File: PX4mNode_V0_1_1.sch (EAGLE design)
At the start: 128 parts, among them J201 DF13C-6P-1.25V, J202 DF13C-6P-1.25V, J203 DF13C-6P-1.25V, J301 DF13C-4P-1.25V, J401 DF13C-7P-1.25V, J402 DF13-4P-1.25V, J403 DF13C-4P-1.25V, J404 DF13C-4P-1.25V, J405 DF13C-4P-1.25V, J801 DF13C-3P-1.25V, M3_MOUNT1101 MOUNT-HOLE3.1MM, M3_MOUNT1102 MOUNT-HOLE3.1MM, M3_MOUNT1103 MOUNT-HOLE3.1MM, M3_MOUNT1104 MOUNT-HOLE3.1MM, U101 STM32F4X7VX, U401 MAX3051, U402 MAX3051, X101 3.2x2.5 mm / 24 MHz / 15 ppm

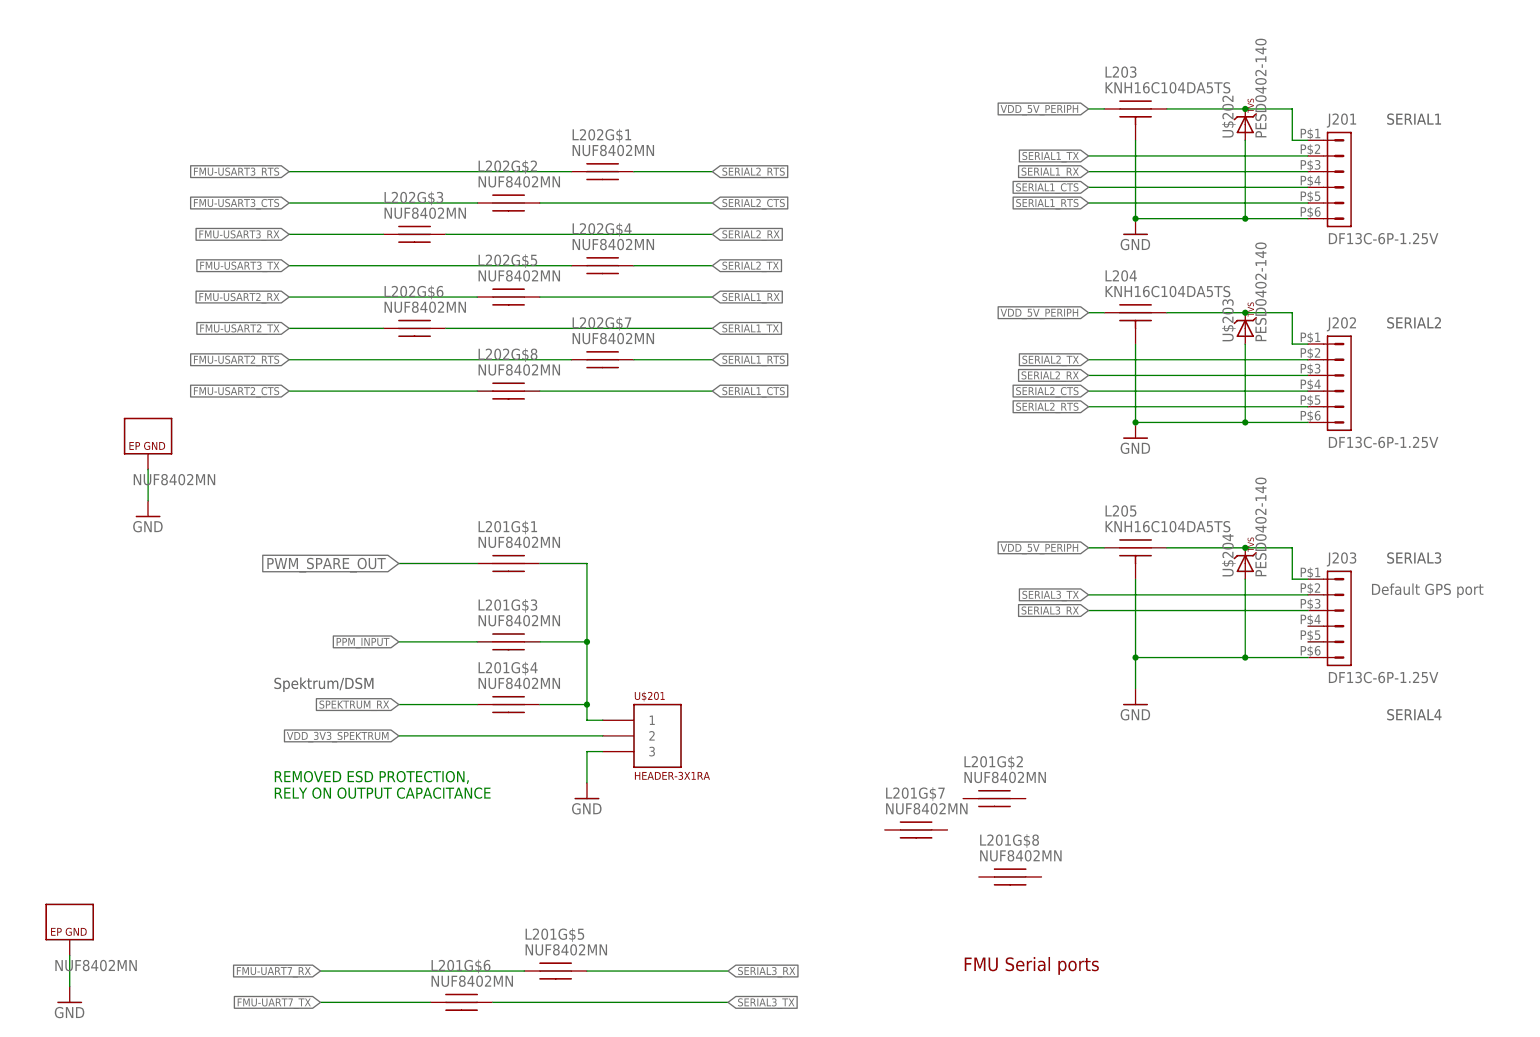
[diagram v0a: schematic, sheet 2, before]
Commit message: Added SBUS input inverter
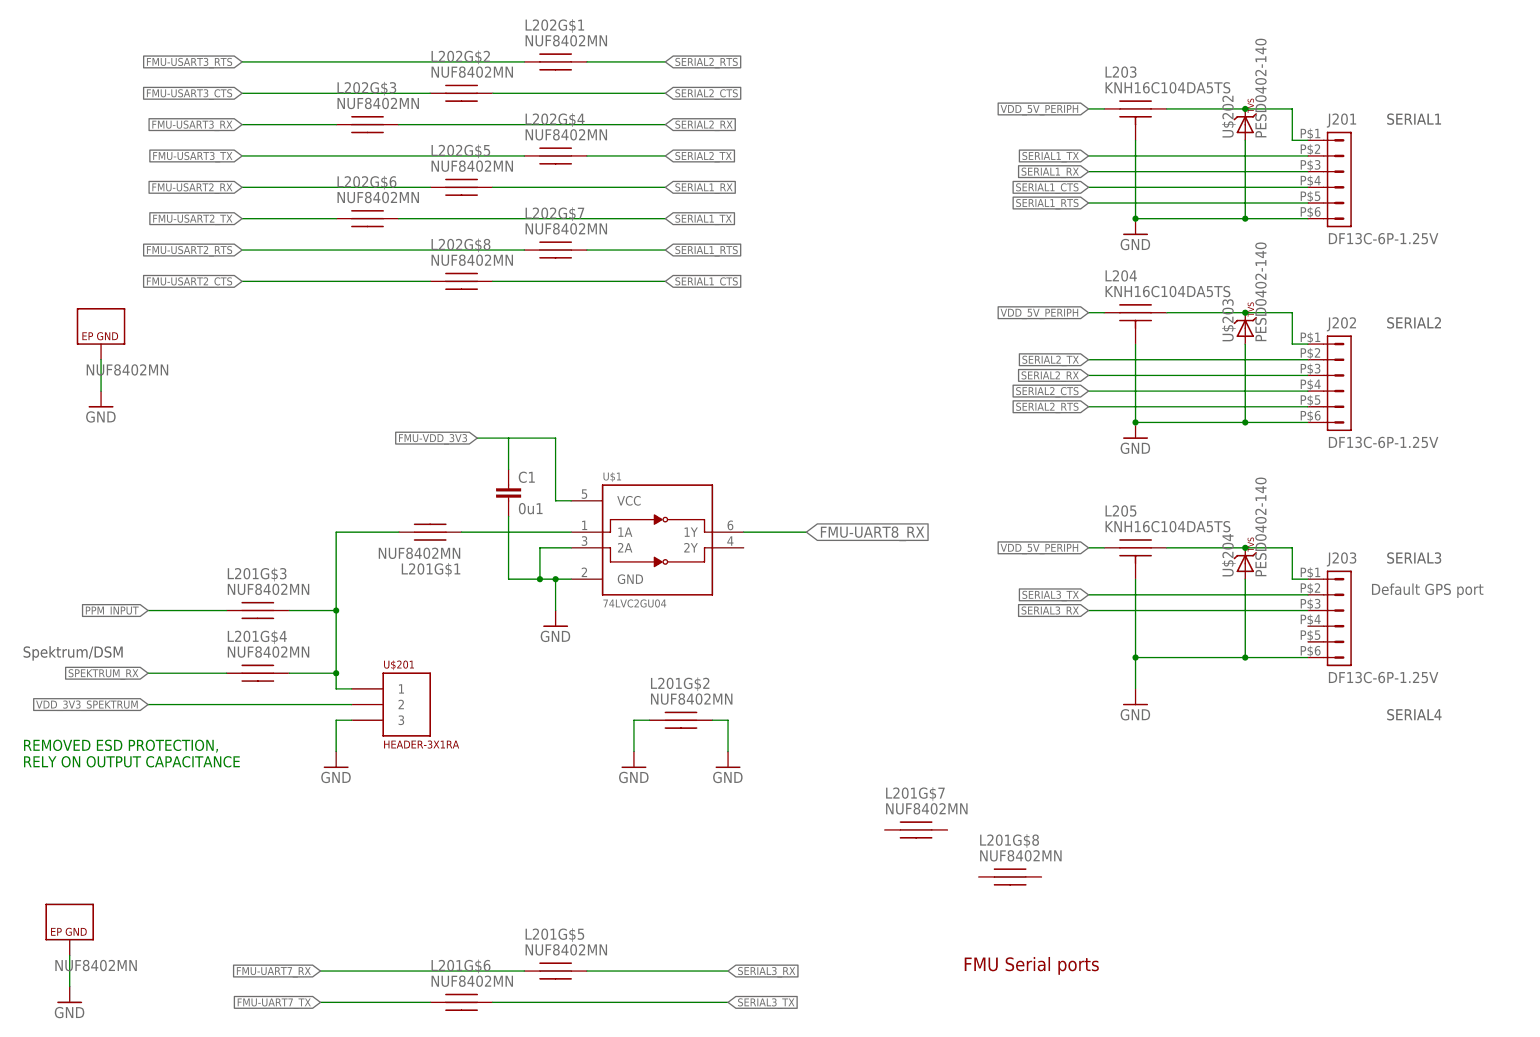
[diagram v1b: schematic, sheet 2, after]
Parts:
- added C1: 0u1, pixhawk2:CAP0402
- added U$1: 74LVC2GU04, pixhawk2:74LVC2GU04
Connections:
- removed net PWM_SPARE_OUT: L201G$1.P$1
- new net N$5: L201G$1.P$1, U$1.1A
- net FMU-UART8_RX: now also U$1.1Y
- net FMU-VDD_3V3: now also C1.1, U$1.VCC
- net GND: now also C1.2, L201G$2.P$1, L201G$2.P$2, U$1.2A, U$1.GND
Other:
- moved on the sheet: L201G$1, L201G$2, L201G$3, L201G$4, L202G$1, L202G$2, L202G$3, L202G$4, L202G$5, L202G$6, L202G$7, L202G$8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

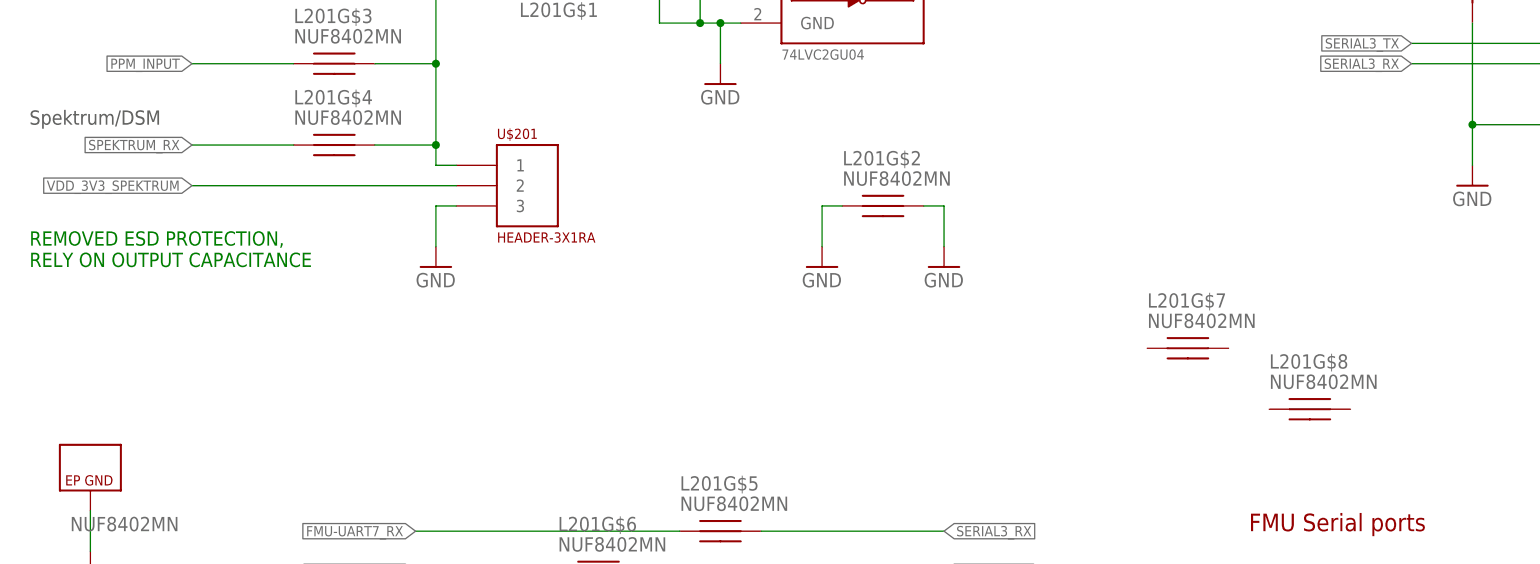
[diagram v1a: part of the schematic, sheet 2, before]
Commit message: Added power selector for PPM/Spektrum/SBUS power output
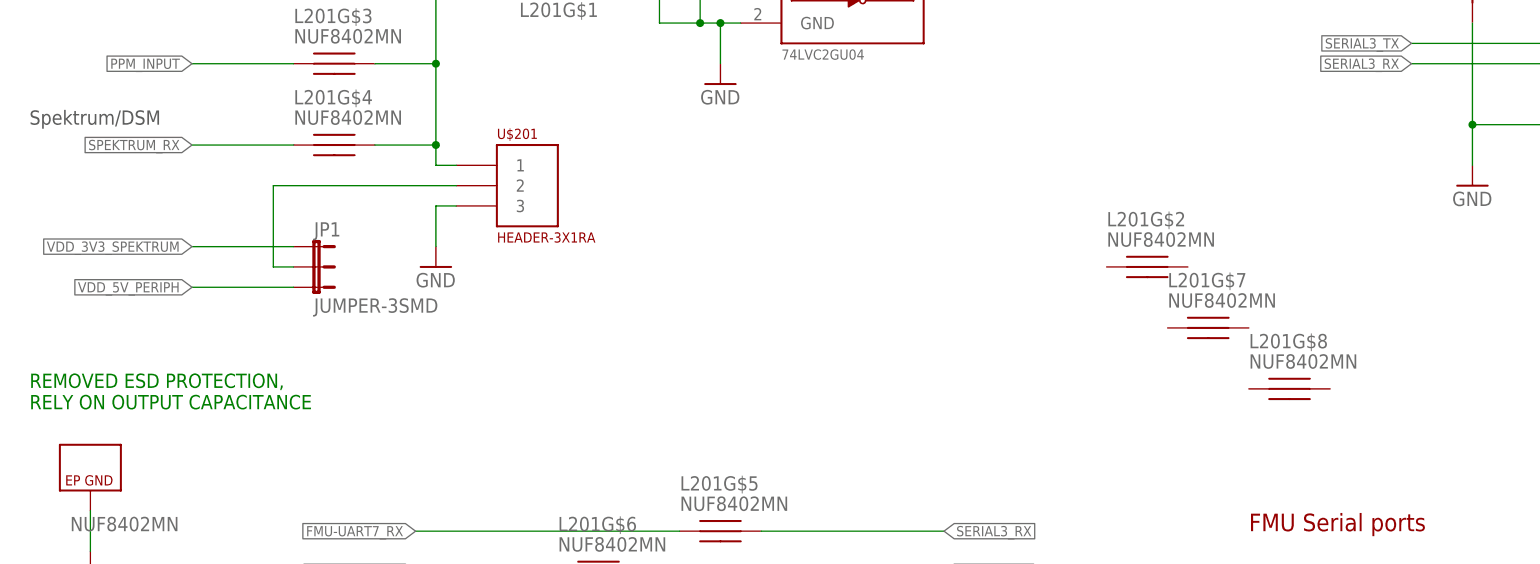
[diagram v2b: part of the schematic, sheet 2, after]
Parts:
- added JP1: JUMPER-3SMD, SparkFun-Passives:JUMPER-3SMD
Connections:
- new net VDD_RX_POWER: JP1.2, U$201.2
- net GND: no longer L201G$2.P$1, L201G$2.P$2
- net VDD_3V3_SPEKTRUM: now also JP1.1; no longer U$201.2
- net VDD_5V_PERIPH: now also JP1.3
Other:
- moved on the sheet: L201G$2, L201G$7, L201G$8
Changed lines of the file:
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@@
 <attribute name="PARTNO" value="CC0402ZRY5V7BB104"/>
 </part>
-<part name="GND19" library="pixhawk2" deviceset="GND" device=""/>
-<part name="GND22" library="pixhawk2" deviceset="GND" device=""/>
+<part name="JP1" library="SparkFun-Passives" deviceset="JUMPER-3" device="SMD"/>
 </parts>
 <sheets>
@@
 <text x="231.14" y="78.74" size="1.778" layer="95">Default GPS port</text>
 <text x="12.7" y="68.58" size="1.778" layer="97">Spektrum/DSM</text>
-<text x="12.7" y="50.8" size="1.778" layer="91">REMOVED ESD PROTECTION,
+<text x="12.7" y="33.02" size="1.778" layer="91">REMOVED ESD PROTECTION,
 RELY ON OUTPUT CAPACITANCE</text>
 </plain>
@@
 <instance part="U$201" gate="G$1" x="73.66" y="58.42"/>
 <instance part="L201" gate="G$1" x="78.74" y="88.9" rot="R180"/>
-<instance part="L201" gate="G$2" x="119.38" y="58.42"/>
-<instance part="L201" gate="G$7" x="157.48" y="40.64"/>
-<instance part="L201" gate="G$8" x="172.72" y="33.02"/>
+<instance part="L201" gate="G$7" x="160.02" y="43.18"/>
+<instance part="L201" gate="G$2" x="152.4" y="50.8"/>
+<instance part="L201" gate="G$8" x="170.18" y="35.56"/>
 <instance part="U$1" gate="G$1" x="114.3" y="86.36"/>
 <instance part="GND2" gate="1" x="99.06" y="73.66"/>
@@
 <attribute name="PARTNO" x="91.44" y="93.98" size="1.778" layer="96" display="off"/>
 </instance>
-<instance part="GND19" gate="1" x="111.76" y="50.8"/>
-<instance part="GND22" gate="1" x="127" y="50.8"/>
+<instance part="JP1" gate="G$1" x="48.26" y="53.34" rot="R270"/>
 </instances>
 <busses>
@@
 <junction x="96.52" y="81.28"/>
 </segment>
-<segment>
-<pinref part="GND19" gate="1" pin="GND"/>
-<wire x1="111.76" y1="53.34" x2="111.76" y2="58.42" width="0.1524" layer="91"/>
-<pinref part="L201" gate="G$2" pin="P$1"/>
-<wire x1="111.76" y1="58.42" x2="114.3" y2="58.42" width="0.1524" layer="91"/>
-</segment>
-<segment>
-<pinref part="L201" gate="G$2" pin="P$2"/>
-<wire x1="124.46" y1="58.42" x2="127" y2="58.42" width="0.1524" layer="91"/>
-<pinref part="GND22" gate="1" pin="GND"/>
-<wire x1="127" y1="58.42" x2="127" y2="53.34" width="0.1524" layer="91"/>
-</segment>
 </net>
 <net name="VDD_5V_PERIPH" class="1">
@@
 <label x="185.42" y="157.48" size="1.27" layer="95" rot="R180" xref="yes"/>
 </segment>
+<segment>
+<wire x1="45.72" y1="48.26" x2="33.02" y2="48.26" width="0.1524" layer="91"/>
+<label x="33.02" y="48.26" size="1.27" layer="95" rot="R180" xref="yes"/>
+<pinref part="JP1" gate="G$1" pin="3"/>
+</segment>
 </net>
 <net name="SPEKTRUM_RX" class="0">
@@
 <net name="VDD_3V3_SPEKTRUM" class="1">
 <segment>
-<label x="33.02" y="60.96" size="1.27" layer="95" rot="R180" xref="yes"/>
-<pinref part="U$201" gate="G$1" pin="2"/>
-<wire x1="66.04" y1="60.96" x2="33.02" y2="60.96" width="0.1524" layer="91"/>
+<label x="33.02" y="53.34" size="1.27" layer="95" rot="R180" xref="yes"/>
+<pinref part="JP1" gate="G$1" pin="1"/>
+<wire x1="45.72" y1="53.34" x2="33.02" y2="53.34" width="0.1524" layer="91"/>
 </segment>
 </net>
@@
 </segment>
 </net>
+<net name="VDD_RX_POWER" class="0">
+<segment>
+<pinref part="JP1" gate="G$1" pin="2"/>
+<wire x1="45.72" y1="50.8" x2="43.18" y2="50.8" width="0.1524" layer="91"/>
+<wire x1="43.18" y1="50.8" x2="43.18" y2="60.96" width="0.1524" layer="91"/>
+<pinref part="U$201" gate="G$1" pin="2"/>
+<wire x1="43.18" y1="60.96" x2="66.04" y2="60.96" width="0.1524" layer="91"/>
+</segment>
+</net>

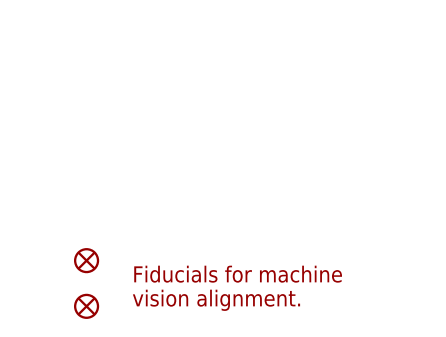
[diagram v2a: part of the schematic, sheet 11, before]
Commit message: Added fiducials to bottom side to support fine pitch packages
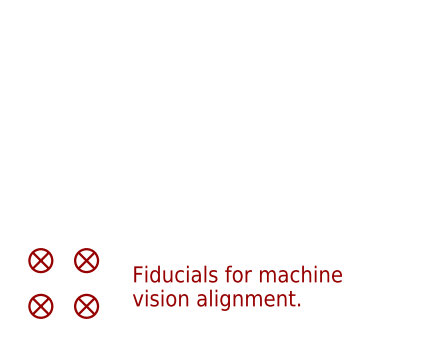
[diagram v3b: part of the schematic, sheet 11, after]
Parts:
- added JP2, JP3: FIDUCIAL1.5X3, pixhawk2:FIDUCIAL1.5X3
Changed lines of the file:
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@@
 </part>
 <part name="JP1" library="SparkFun-Passives" deviceset="JUMPER-3" device="SMD"/>
+<part name="JP2" library="pixhawk2" deviceset="FIDUCIAL" device="1.5X3">
+<attribute name="BOM" value="EXCLUDE"/>
+<attribute name="PARTNO" value="*"/>
+</part>
+<part name="JP3" library="pixhawk2" deviceset="FIDUCIAL" device="1.5X3">
+<attribute name="BOM" value="EXCLUDE"/>
+<attribute name="PARTNO" value="*"/>
+</part>
 </parts>
 <sheets>
@@
 <attribute name="BOM" x="20.32" y="12.7" size="1.778" layer="96" display="off"/>
 </instance>
+<instance part="JP2" gate="G$1" x="15.24" y="17.78">
+<attribute name="PARTNO" x="15.24" y="17.78" size="1.778" layer="96" display="off"/>
+<attribute name="BOM" x="15.24" y="17.78" size="1.778" layer="96" display="off"/>
+</instance>
+<instance part="JP3" gate="G$1" x="15.24" y="12.7">
+<attribute name="PARTNO" x="15.24" y="12.7" size="1.778" layer="96" display="off"/>
+<attribute name="BOM" x="15.24" y="12.7" size="1.778" layer="96" display="off"/>
+</instance>
 </instances>
